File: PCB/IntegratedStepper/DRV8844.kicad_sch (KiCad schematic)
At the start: 16 parts, among them IC1 DRV8844PWPR

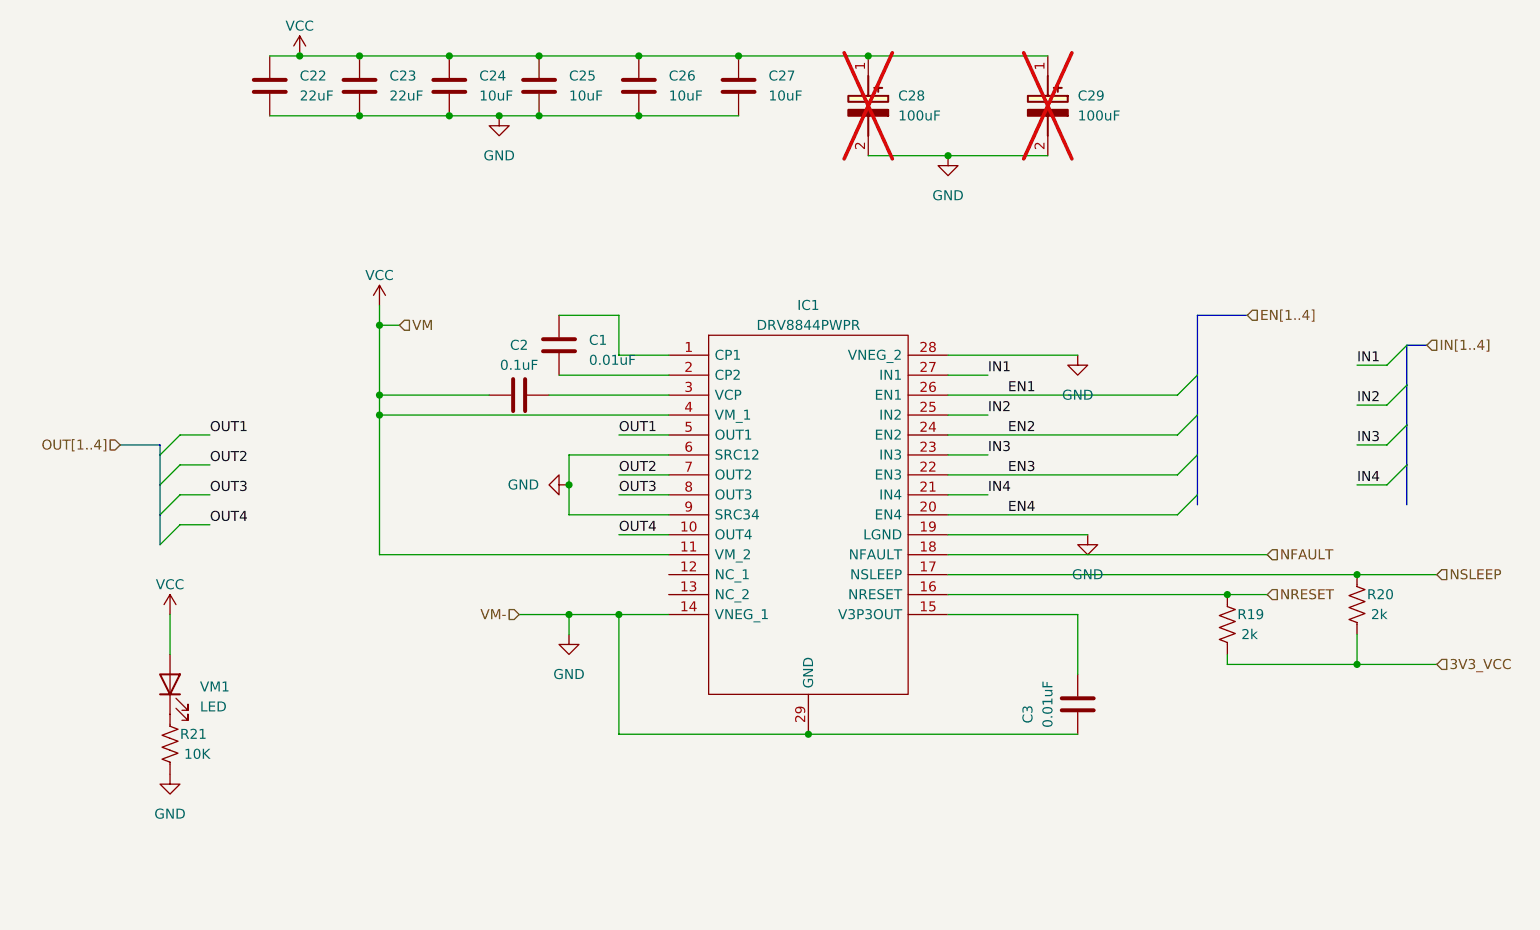
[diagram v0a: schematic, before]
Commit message: Update PCB with DRV8243 for 12A capacity
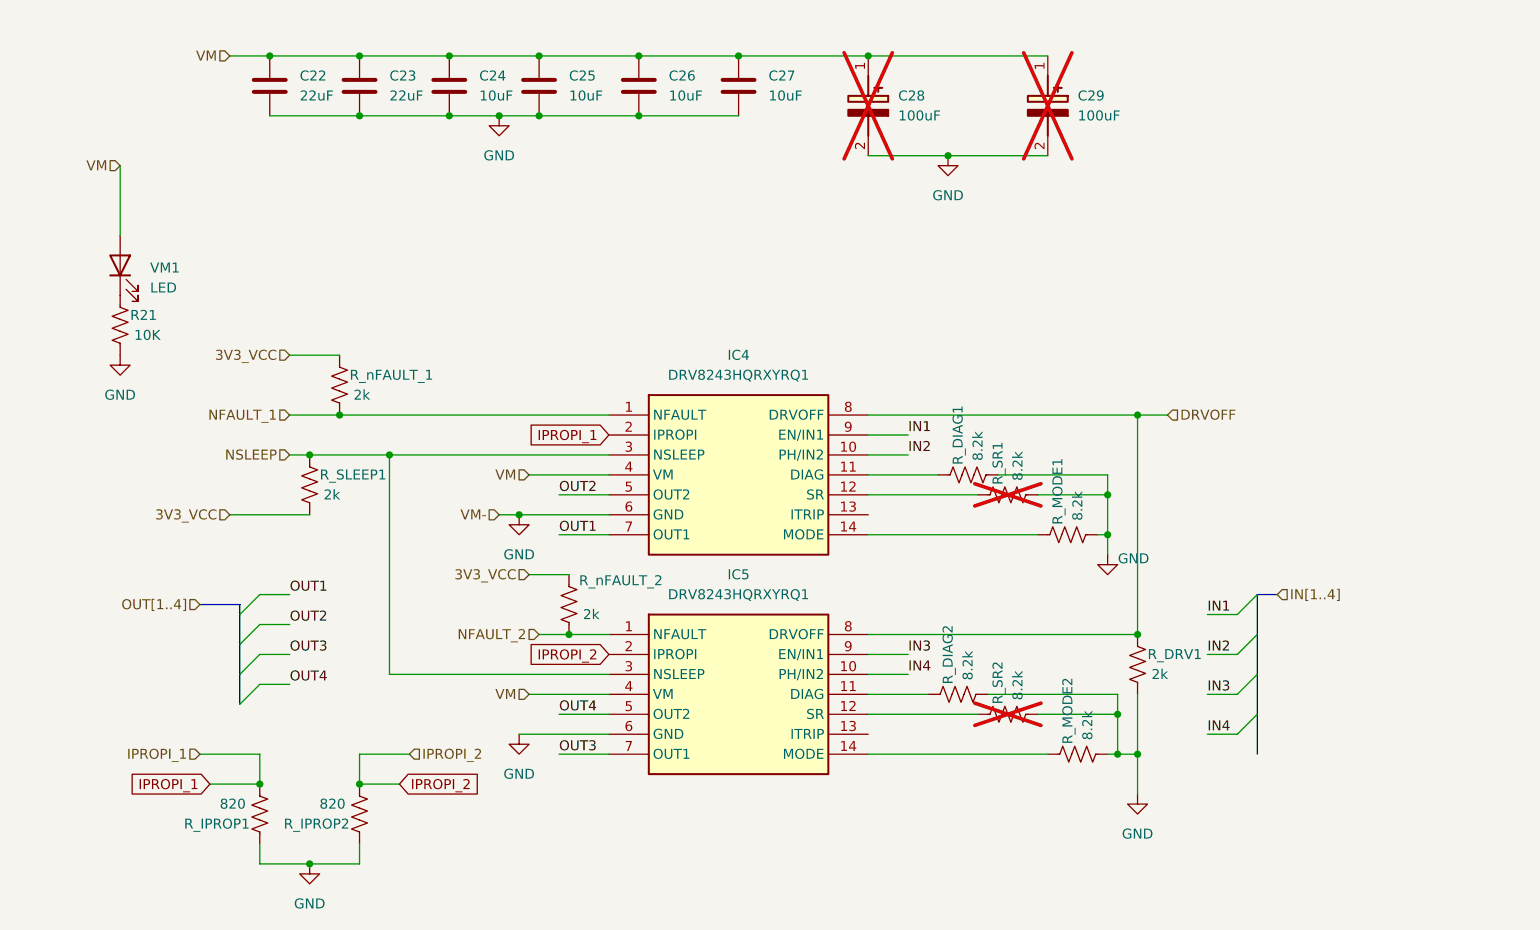
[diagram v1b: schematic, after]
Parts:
- removed C1, C3: 0.01uF, Capacitor_SMD:C_0805_2012Metric, symbol Device:C
- removed C2: 0.1uF, Capacitor_SMD:C_0805_2012Metric, symbol Device:C
- removed IC1: DRV8844PWPR, SamacSys_Parts:SOP65P640X120-29N, symbol SamacSys_Parts:DRV8844PWPR
- removed R19, R20: 2k, Resistor_SMD:R_0603_1608Metric, symbol Device:R_US
- added IC4, IC5: DRV8243HQRXYRQ1, SamacSys_Parts:DRV8243HQRXYRQ1, symbol SamacSys_Parts:DRV8243HQRXYRQ1
- added R_DIAG1, R_DIAG2, R_MODE1, R_MODE2, R_SR1, R_SR2: 8.2k, Resistor_SMD:R_0603_1608Metric, symbol Device:R_US
- added R_DRV1, R_SLEEP1, R_nFAULT_1, R_nFAULT_2: 2k, Resistor_SMD:R_0603_1608Metric, symbol Device:R_US
- added R_IPROP1, R_IPROP2: 820, Resistor_SMD:R_0603_1608Metric, symbol Device:R_US
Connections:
- net 3V3_VCC: now also R_SLEEP1.1, R_nFAULT_1.2, R_nFAULT_2.2
- net GND: now also IC4.6 (GND), IC5.6 (GND), R_DIAG1.1, R_DIAG2.1, R_DRV1.1, R_IPROP1.2, R_IPROP2.2, R_MODE1.1, R_MODE2.1, R_SR1.1, R_SR2.1
- net IN1: now also IC4.9 (EN/IN1)
- net IN2: now also IC4.10 (PH/IN2)
- net IN3: now also IC5.9 (EN/IN1)
- net IN4: now also IC5.10 (PH/IN2)
- net NSLEEP: now also IC4.3 (NSLEEP), IC5.3 (NSLEEP), R_SLEEP1.2
- net OUT1: now also IC4.7 (OUT1)
- net OUT2: now also IC4.5 (OUT2)
- net OUT3: now also IC5.7 (OUT1)
- net OUT4: now also IC5.5 (OUT2)
- net VCC renamed VM
- net VM: now also IC4.4 (VM), IC5.4 (VM)
- new net: IC4.12 (SR), R_SR1.2
- new net: IC4.11 (DIAG), R_DIAG1.2
- new net: IC4.14 (MODE), R_MODE1.2
- new net: IC5.12 (SR), R_SR2.2
- new net: IC5.11 (DIAG), R_DIAG2.2
- new net: IC5.14 (MODE), R_MODE2.2
- new net DRVOFF: IC4.8 (DRVOFF), IC5.8 (DRVOFF), R_DRV1.2
- new net IPROPI_1: IC4.2 (IPROPI), R_IPROP1.1
- new net IPROPI_2: IC5.2 (IPROPI), R_IPROP2.1
- new net NFAULT_1: IC4.1 (NFAULT), R_nFAULT_1.1
- new net NFAULT_2: IC5.1 (NFAULT), R_nFAULT_2.1
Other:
- moved on the sheet: R21, VM1

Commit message: update layout temp
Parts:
- removed C22: 22uF, Capacitor_SMD:C_1210_3225Metric, symbol Device:C
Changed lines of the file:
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@@
 	)
 	(junction
-		(at 92.71 36.83)
-		(diameter 0)
-		(color 0 0 0 0)
-	)
-	(junction
 		(at 189.23 118.11)
 		(diameter 0)
@@
 	)
 	(junction
-		(at 81.28 29.21)
-		(diameter 0)
-		(color 0 0 0 0)
-	)
-	(junction
 		(at 187.96 85.09)
 		(diameter 0)
@@
 	(wire
 		(pts
-			(xy 81.28 29.21) (xy 92.71 29.21)
+			(xy 76.2 29.21) (xy 92.71 29.21)
 		)
 		(stroke
@@
 	(wire
 		(pts
-			(xy 81.28 36.83) (xy 92.71 36.83)
-		)
-		(stroke
-			(width 0)
-			(type default)
-		)
-	)
-	(wire
-		(pts
 			(xy 86.36 80.01) (xy 83.82 80.01)
 		)
@@
 	(wire
 		(pts
-			(xy 76.2 29.21) (xy 81.28 29.21)
-		)
-		(stroke
-			(width 0)
-			(type default)
-		)
-	)
-	(wire
-		(pts
 			(xy 115.57 102.87) (xy 119.38 102.87)
 		)
@@
 					(unit 1)
 				)
-			)
-		)
-	)
-	(symbol
-		(lib_id "Device:C")
-		(at 81.28 33.02 0)
-		(unit 1)
-		(exclude_from_sim no)
-		(in_bom yes)
-		(on_board yes)
-		(dnp no)
-		(fields_autoplaced yes)
-		(property "Reference" "C22"
-			(at 85.09 31.7499 0)
-			(effects
-				(font
-					(size 1.27 1.27)
-				)
-				(justify left)
-			)
-		)
-		(property "Value" "22uF"
-			(at 85.09 34.2899 0)
-			(effects
-				(font
-					(size 1.27 1.27)
-				)
-				(justify left)
-			)
-		)
-		(property "Footprint" "Capacitor_SMD:C_1210_3225Metric"
-			(at 82.2452 36.83 0)
-			(effects
-				(font
-					(size 1.27 1.27)
-				)
-				(hide yes)
-			)
-		)
-		(property "Datasheet" "~"
-			(at 81.28 33.02 0)
-			(effects
-				(font
-					(size 1.27 1.27)
-				)
-				(hide yes)
-			)
-		)
-		(property "Description" "Unpolarized capacitor"
-			(at 81.28 33.02 0)
-			(effects
-				(font
-					(size 1.27 1.27)
-				)
-				(hide yes)
-			)
-		)
-		(property "Voltage Rating" "100V"
-			(at 81.28 33.02 0)
-			(effects
-				(font
-					(size 1.27 1.27)
-				)
-				(hide yes)
-			)
-		)
-		(property "LCSC" "C2929200"
-			(at 81.28 33.02 0)
-			(effects
-				(font
-					(size 1.27 1.27)
-				)
-				(hide yes)
-			)
-		)
-		(property "LCSC Part Number" "C2929200"
-			(at 81.28 33.02 0)
-			(effects
-				(font
-					(size 1.27 1.27)
-				)
-				(hide yes)
-			)
-		)
-		(pin "1"
-		)
-		(pin "2"
-		)
-		(instances
-			(project "IntegratedStepper"
-				(path "/ab592993-dafc-411a-b466-8e8425f43767/629c76d2-6f66-4ca5-9833-9cfbfc13e6ac"
-					(reference "C22")
-					(unit 1)
-				)

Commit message: update layout with pinout changes
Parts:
- removed C28, C29: 100uF, CAPPRD350W65D800H1650, symbol SamacSys_Parts:EEU-FC1J101LB
